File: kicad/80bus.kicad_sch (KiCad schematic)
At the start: 8 parts, among them SW1 SW_SPST, U1 4049

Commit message: Silkscreen tidy
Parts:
- R2: value 680 -> 1K
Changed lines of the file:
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@@
   (title_block
     (title "EPROM Burner 2708 / 2716")
-    (date "2023-05-21")
-    (rev "2.1")
+    (date "2023-06-21")
+    (rev "2.3")
   )
   (junction (at 58.42 157.48) (diameter 0) (color 0 0 0 0)
@@
       (effects (font (size 1.27 1.27)) (justify left))
     )
-    (property "Value" "680" (at 175.26 92.075 0)
+    (property "Value" "1K" (at 175.26 92.075 0)
       (effects (font (size 1.27 1.27)) (justify left))
     )

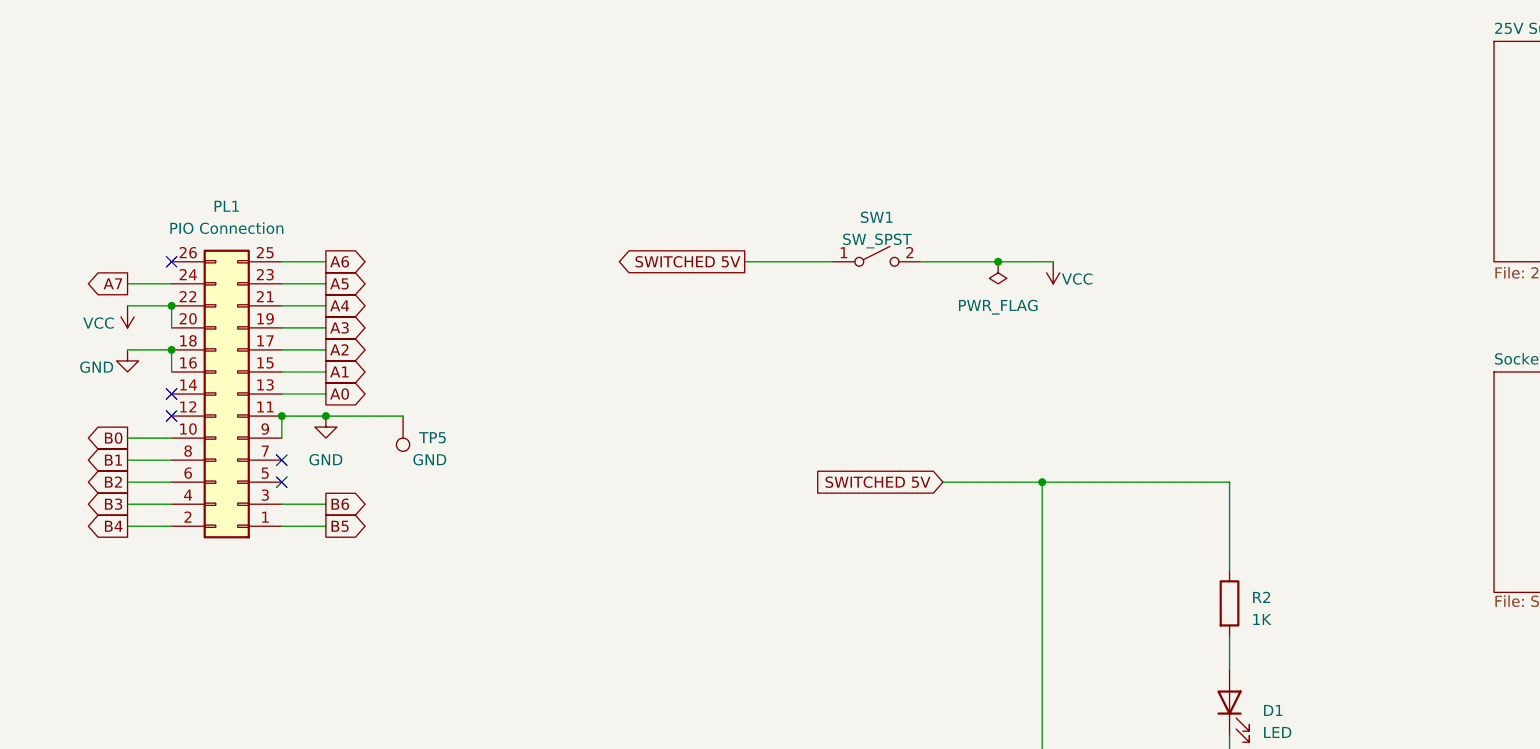
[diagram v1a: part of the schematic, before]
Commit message: Add aux power feeds
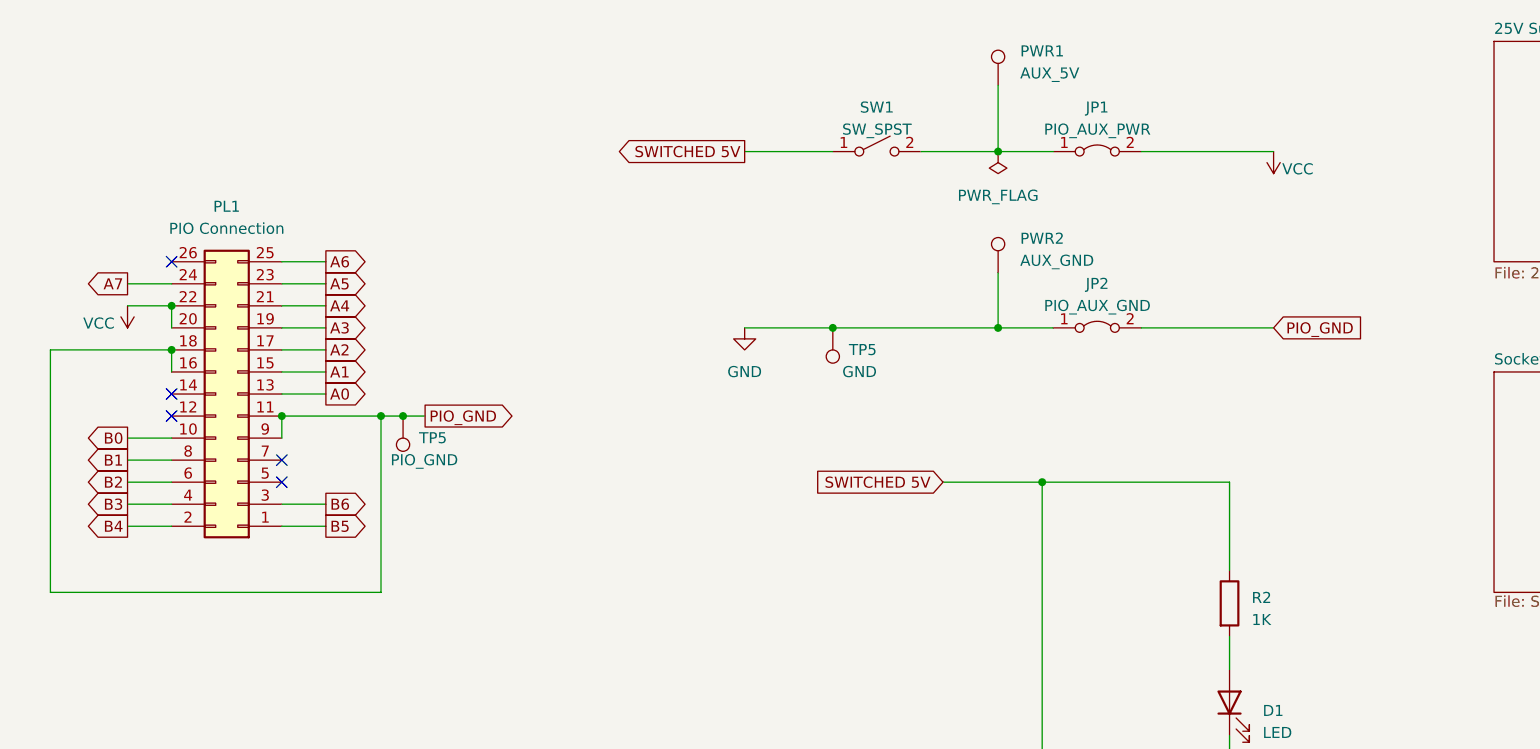
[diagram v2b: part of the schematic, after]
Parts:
- added JP1: PIO_AUX_PWR, Connector_PinHeader_2.54mm:PinHeader_1x02_P2.54mm_Vertical, symbol Jumper:Jumper_2_Bridged
- added JP2: PIO_AUX_GND, Connector_PinHeader_2.54mm:PinHeader_1x02_P2.54mm_Vertical, symbol Jumper:Jumper_2_Bridged
- added PWR1: AUX_5V, TestPoint:TestPoint_THTPad_4.0x4.0mm_Drill2.0mm, symbol Connector:TestPoint
- added PWR2: AUX_GND, TestPoint:TestPoint_THTPad_4.0x4.0mm_Drill2.0mm, symbol Connector:TestPoint
- added TP5: GND, TestPoint:TestPoint_THTPad_2.0x2.0mm_Drill1.0mm, symbol Connector:TestPoint
- TP5: value GND -> PIO_GND
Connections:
- net GND: now also JP2.1 (A), PWR2.1, TP5.1; no longer PL1.11 (Pin_11), PL1.16 (Pin_16), PL1.18 (Pin_18), PL1.9 (Pin_9), TP5.1
- net VCC: now also JP1.2 (B); no longer SW1.2 (B)
- new net: JP1.1 (A), PWR1.1, SW1.2 (B)
- new net PIO_GND: JP2.2 (B), PL1.11 (Pin_11), PL1.16 (Pin_16), PL1.18 (Pin_18), PL1.9 (Pin_9), TP5.1
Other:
- moved on the sheet: SW1

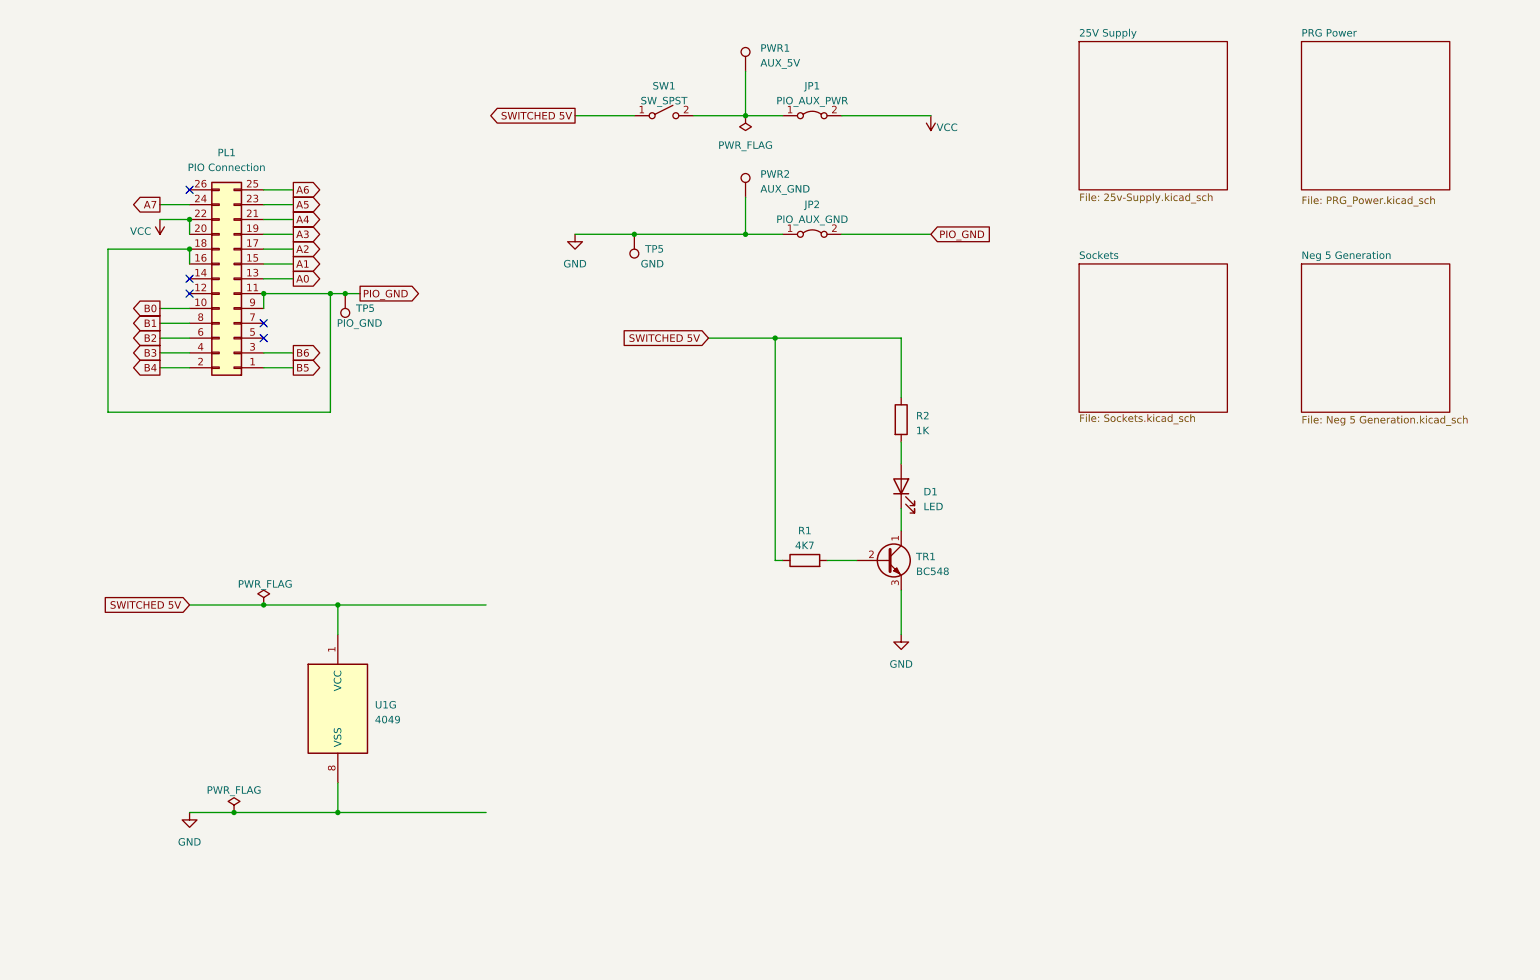
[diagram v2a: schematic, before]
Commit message: Add soft start
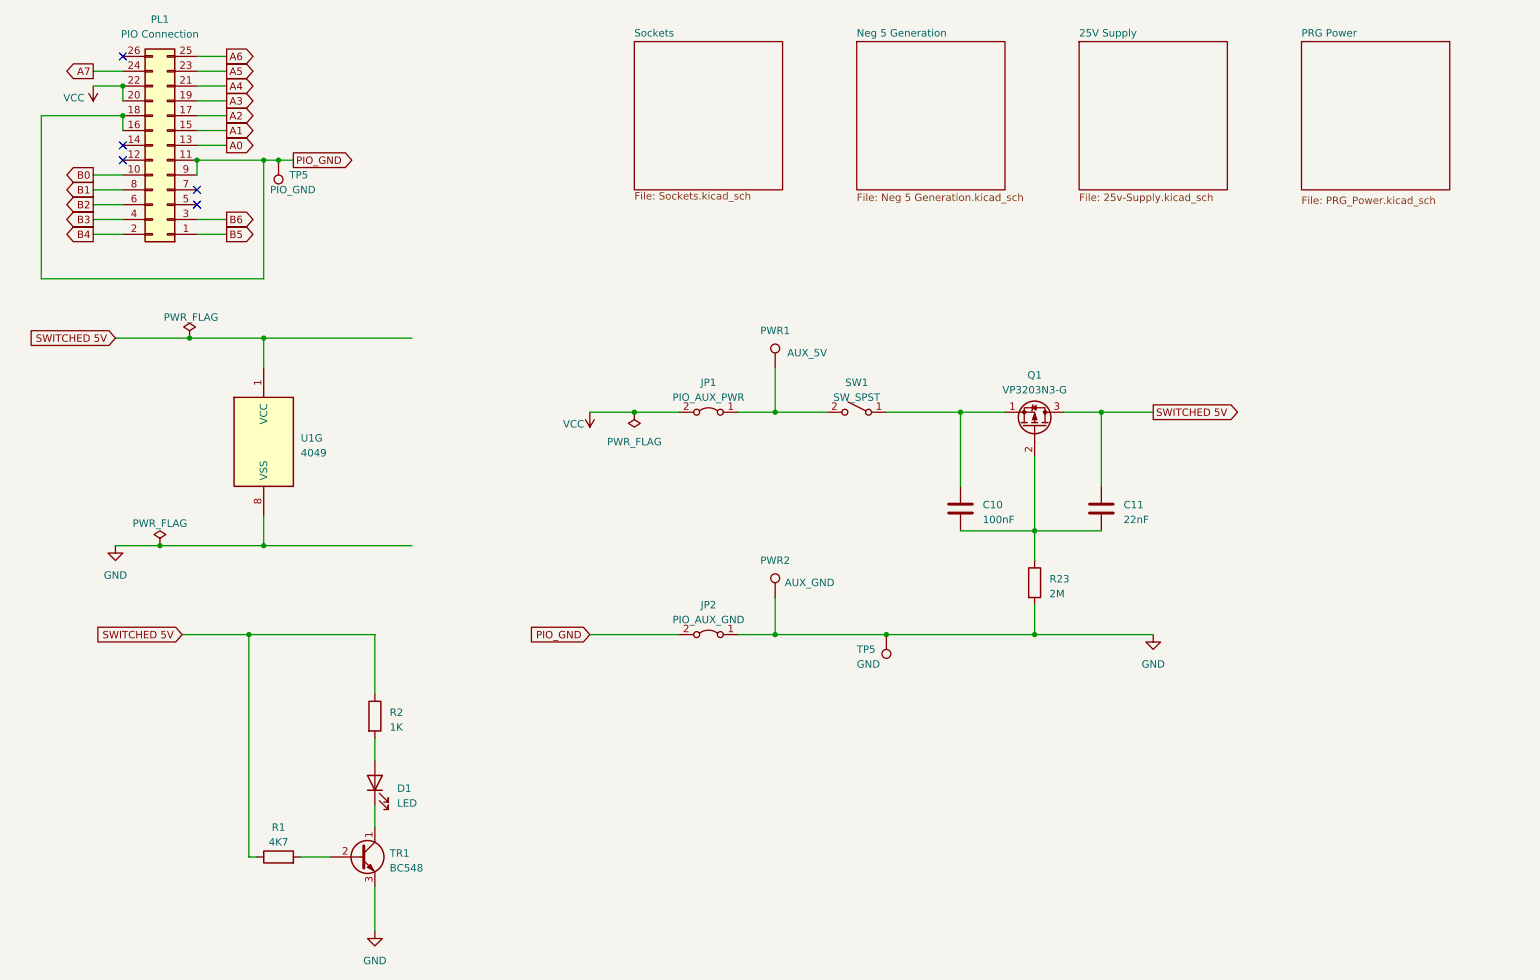
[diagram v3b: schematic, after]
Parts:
- added C10: 100nF, Capacitor_THT:C_Disc_D5.0mm_W2.5mm_P5.00mm, symbol Device:C
- added C11: 22nF, Capacitor_THT:C_Disc_D5.0mm_W2.5mm_P5.00mm, symbol Device:C
- added Q1: VP3203N3-G, Package_TO_SOT_THT:TO-92L_Inline_Wide, symbol Transistor_FET:VP0610L
- added R23: 2M, Resistor_THT:R_Axial_DIN0309_L9.0mm_D3.2mm_P12.70mm_Horizontal, symbol Device:R
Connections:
- net GND: now also R23.2
- net SWITCHED 5V: now also C11.1, Q1.3 (D); no longer SW1.1 (A)
- new net: C10.1, Q1.1 (S), SW1.1 (A)
- new net: C10.2, C11.2, Q1.2 (G), R23.1
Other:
- moved on the sheet: D1, JP1, JP2, PL1, PWR1, PWR2, R1, R2, SW1, TP5, TR1, U1G

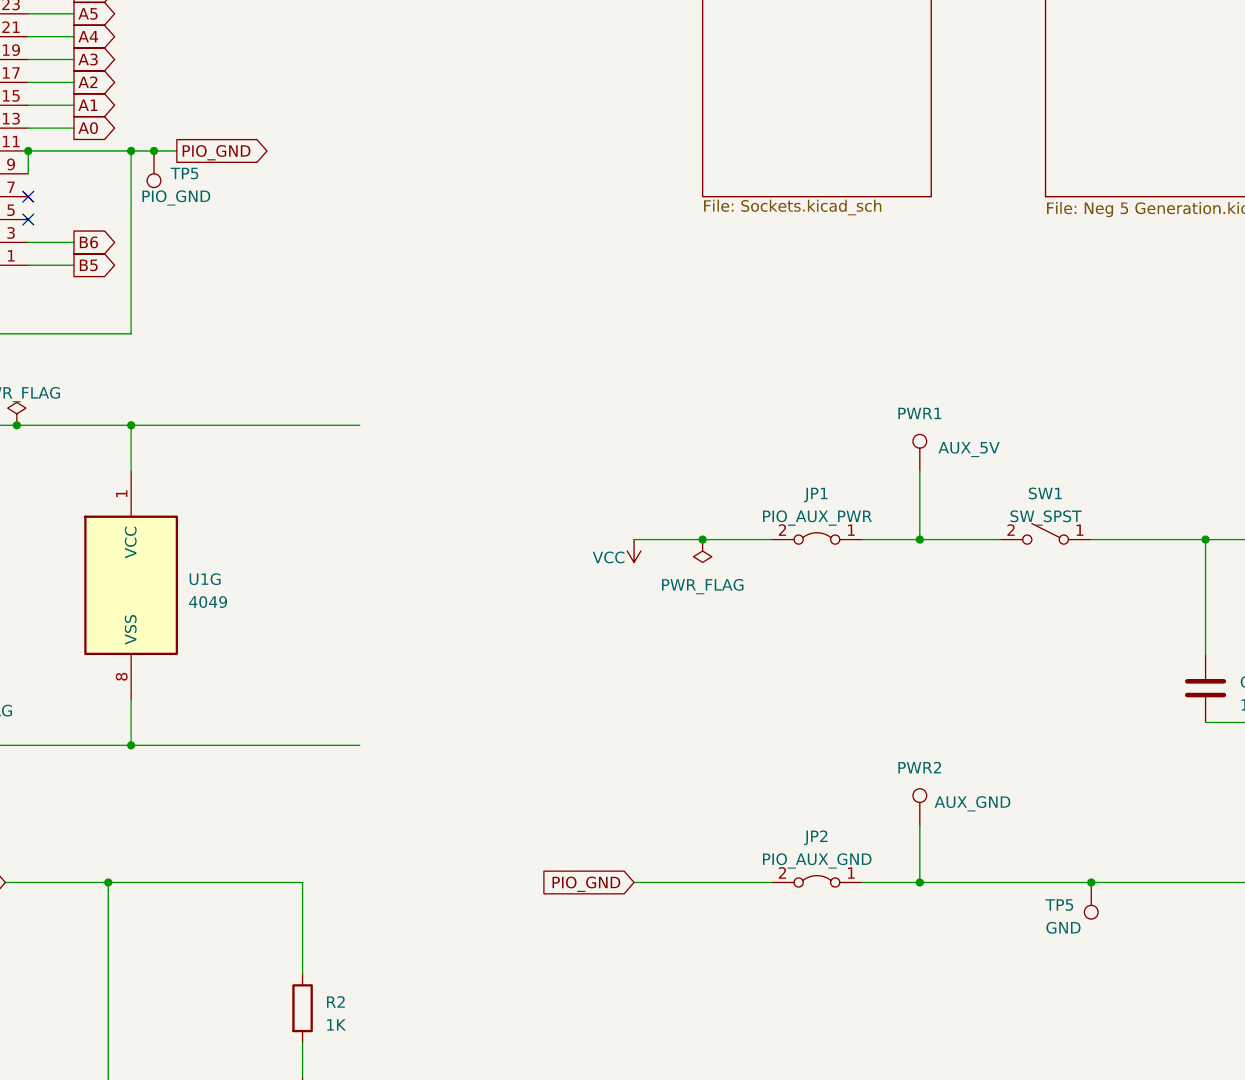
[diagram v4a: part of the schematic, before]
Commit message: Kicad 8, updated docs
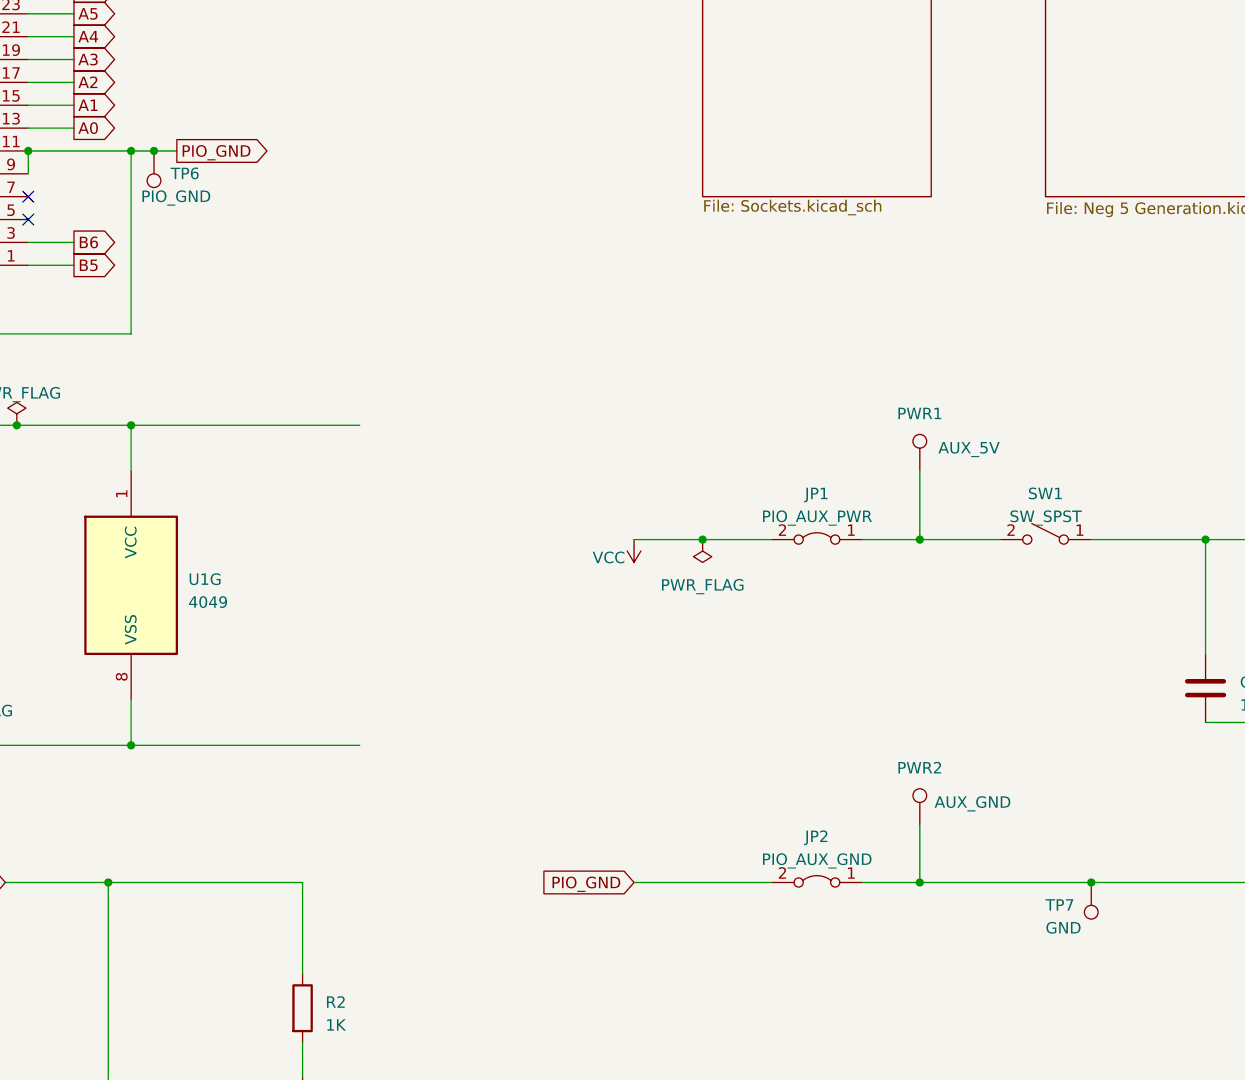
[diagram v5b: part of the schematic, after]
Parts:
- renumbered TP5 to TP6, TP5 to TP7

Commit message: Update docs
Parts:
- removed SW1: SW_SPST, Button_Switch_THT:SW_DIP_SPSTx01_Slide_6.7x4.1mm_W7.62mm_P2.54mm_LowProfile, symbol Switch:SW_SPST
- added SW1: SW_SPDT, Connector_PinHeader_2.54mm:PinHeader_1x03_P2.54mm_Vertical, symbol Switch:SW_SPDT
- Q1: footprint Package_TO_SOT_THT:TO-92L_Inline_Wide -> Package_TO_SOT_THT:TO-92L_Inline
- TR1: footprint Package_TO_SOT_THT:TO-92_Inline_Wide -> Package_TO_SOT_THT:TO-92_Inline
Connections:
- net at C10.1, Q1.1 (S): now also SW1.3 (C)
- net at JP1.1 (A), PWR1.1: now also SW1.2 (B)
- no-connect marks 5 -> 6
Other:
- note added: "2MS1T2B3M2QES"
- note added: "Soft Start"

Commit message: Update footprints
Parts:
- TR1: footprint Package_TO_SOT_THT:TO-92_Inline -> Package_TO_SOT_THT:TO-92_Inline_Wide
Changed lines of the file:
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@@
 			)
 		)
-		(property "Footprint" "Package_TO_SOT_THT:TO-92_Inline"
+		(property "Footprint" "Package_TO_SOT_THT:TO-92_Inline_Wide"
 			(at 85.09 167.005 0)
 			(effects
